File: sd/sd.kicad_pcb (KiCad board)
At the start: 2 copper layers, 76.2 x 50.8 mm, 13 parts, among them J1 Micro_SD_Card_Det2, J2 Conn_01x09, J3 STM32WORLD_BOARD, J4 STM32WORLD_CONNECTOR_1, J5 STM32WORLD_CONNECTOR_2

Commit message: Working on sd
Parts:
- removed J2: Conn_01x09, Connector_PinHeader_2.54mm:PinHeader_1x09_P2.54mm_Vertical
- added JP1: SolderJumper_3_Open, Jumper:SolderJumper-3_P2.0mm_Open_TrianglePad1.0x1.5mm, F.Cu at (171.5, 87.6)
- added JP10: SolderJumper_2_Open, Jumper:SolderJumper-2_P1.3mm_Open_TrianglePad1.0x1.5mm, F.Cu at (151.1, 87.6)
- added JP11: SolderJumper_2_Open, Jumper:SolderJumper-2_P1.3mm_Open_TrianglePad1.0x1.5mm, F.Cu at (139.7, 97.2)
- added JP12: SolderJumper_2_Open, Jumper:SolderJumper-2_P1.3mm_Open_TrianglePad1.0x1.5mm, F.Cu at (143.5, 97.2)
- added JP13: SolderJumper_2_Open, Jumper:SolderJumper-2_P1.3mm_Open_TrianglePad1.0x1.5mm, F.Cu at (147.3, 97.2)
- added JP14: SolderJumper_2_Open, Jumper:SolderJumper-2_P1.3mm_Open_TrianglePad1.0x1.5mm, F.Cu at (151.1, 97.2)
- added JP15: SolderJumper_2_Open, Jumper:SolderJumper-2_P1.3mm_Open_TrianglePad1.0x1.5mm, F.Cu at (139.7, 92.3)
- added JP16: SolderJumper_2_Open, Jumper:SolderJumper-2_P1.3mm_Open_TrianglePad1.0x1.5mm, F.Cu at (143.5, 92.3)
- added JP17: SolderJumper_2_Open, Jumper:SolderJumper-2_P1.3mm_Open_TrianglePad1.0x1.5mm, F.Cu at (147.3, 92.3)
- added JP18: SolderJumper_2_Open, Jumper:SolderJumper-2_P1.3mm_Open_TrianglePad1.0x1.5mm, F.Cu at (151.1, 92.3)
- added JP19: SolderJumper_2_Open, Jumper:SolderJumper-2_P1.3mm_Open_TrianglePad1.0x1.5mm, F.Cu at (139.7, 101.6)
- added JP2: SolderJumper_3_Open, Jumper:SolderJumper-3_P2.0mm_Open_TrianglePad1.0x1.5mm, F.Cu at (171.5, 90.8)
- added JP20: SolderJumper_2_Open, Jumper:SolderJumper-2_P1.3mm_Open_TrianglePad1.0x1.5mm, F.Cu at (143.5, 101.6)
- added JP21: SolderJumper_2_Open, Jumper:SolderJumper-2_P1.3mm_Open_TrianglePad1.0x1.5mm, F.Cu at (147.3, 101.6)
- added JP22: SolderJumper_2_Open, Jumper:SolderJumper-2_P1.3mm_Open_TrianglePad1.0x1.5mm, F.Cu at (151.1, 101.6)
- added JP3: SolderJumper_3_Open, Jumper:SolderJumper-3_P2.0mm_Open_TrianglePad1.0x1.5mm, F.Cu at (171.5, 94.0)
- added JP4: SolderJumper_3_Open, Jumper:SolderJumper-3_P2.0mm_Open_TrianglePad1.0x1.5mm, F.Cu at (171.5, 97.2)
- added JP5: SolderJumper_3_Open, Jumper:SolderJumper-3_P2.0mm_Open_TrianglePad1.0x1.5mm, F.Cu at (171.5, 100.3)
- added JP6: SolderJumper_3_Open, Jumper:SolderJumper-3_P2.0mm_Open_TrianglePad1.0x1.5mm, F.Cu at (171.5, 103.5)
- added JP7: SolderJumper_2_Open, Jumper:SolderJumper-2_P1.3mm_Open_TrianglePad1.0x1.5mm, F.Cu at (139.7, 87.6)
- added JP8: SolderJumper_2_Open, Jumper:SolderJumper-2_P1.3mm_Open_TrianglePad1.0x1.5mm, F.Cu at (143.5, 87.6)
- added JP9: SolderJumper_2_Open, Jumper:SolderJumper-2_P1.3mm_Open_TrianglePad1.0x1.5mm, F.Cu at (147.3, 87.5)
- moved R2 40.8 mm to (176.5, 103.5), turned to 180 degrees
- moved R3 38.8 mm to (176.5, 90.8), turned to 180 degrees
- moved R6 38.5 mm to (176.5, 94.0), turned to 0 degrees
- moved R5 37.5 mm to (176.5, 100.3), turned to 180 degrees
- moved C2 35.5 mm to (188.0, 105.4), turned to 180 degrees
- moved R4 35.0 mm to (176.5, 97.2), turned to 180 degrees
- moved R1 34.7 mm to (176.5, 87.6), turned to 180 degrees
- moved C1 32.8 mm to (188.0, 103.5), turned to 180 degrees
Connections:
- J1 pad 1: /D2 -> /SD_DAT2
- J1 pad 10: /DET -> DET
- J1 pad 2: /D3 -> /SD_DAT3
- J1 pad 3: /CMD -> /SD_CMD
- J1 pad 5: /CLK -> /SD_CLK
- J1 pad 7: /D0 -> /SD_DAT0
- J1 pad 8: /D1 -> /SD_DAT1
- J4 pad 1: unconnected-(J4-GND-Pad1) -> GND
- J4 pad 11: unconnected-(J4-PA3-Pad11) -> SPI2_MOSI
- J4 pad 13: unconnected-(J4-PA5-Pad13) -> SPI1_CLK
- J4 pad 14: unconnected-(J4-PA4-Pad14) -> SPI1_CS
- J4 pad 15: unconnected-(J4-PA7-Pad15) -> SPI1_MOSI
- J4 pad 16: unconnected-(J4-PA6-Pad16) -> SPI1_MISO
- J4 pad 24: unconnected-(J4-PB10-Pad24) -> SPI2_CLK
- J4 pad 26: unconnected-(J4-PB12-Pad26) -> SPI2_CS
- J4 pad 31: unconnected-(J4-PC9-Pad31) -> SDIO_DAT1
- J4 pad 32: unconnected-(J4-PC8-Pad32) -> SDIO_DAT0
- J4 pad 37: unconnected-(J4-GND-Pad37) -> GND
- J4 pad 38: unconnected-(J4-3.3V-Pad38) -> VCC
- J4 pad 39: unconnected-(J4-GND-Pad39) -> GND
- J4 pad 8: unconnected-(J4-PC2-Pad8) -> SPI2_MISO
- J5 pad 1: unconnected-(J5-GND-Pad1) -> GND
- J5 pad 15: unconnected-(J5-PA15-Pad15) -> SPI1A_CS
- J5 pad 19: unconnected-(J5-PC11-Pad19) -> SDIO_DAT3
- J5 pad 20: unconnected-(J5-PC10-Pad20) -> SDIO_DAT2
- J5 pad 22: unconnected-(J5-PC12-Pad22) -> SDIO_CLK
- J5 pad 23: unconnected-(J5-PB3-Pad23) -> SPI1A_CLK
- J5 pad 24: unconnected-(J5-PD2-Pad24) -> SDIO_CMD
- J5 pad 25: unconnected-(J5-PB5-Pad25) -> SPI1A_MOSI
- J5 pad 26: unconnected-(J5-PB4-Pad26) -> SPI1A_MISO
- J5 pad 3: unconnected-(J5-GND-Pad3) -> GND
- J5 pad 35: unconnected-(J5-PC15-Pad35) -> DET
- J5 pad 4: unconnected-(J5-3.3V-Pad4) -> VCC
- R1 pad 2: /D2 -> SDIO_DAT2
- R2 pad 2: /D3 -> SDIO_DAT1
- R3 pad 2: /CMD -> /SD_DAT3
- R4 pad 2: /D0 -> /SD_CMD
- R5 pad 2: /D1 -> /SD_DAT0
- R6 pad 2: /DET -> DET
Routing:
- net DET: track 0.00 -> 66.8 mm
- net SDIO_DAT2: track 0.00 -> 49.5 mm, vias 0 -> 2
- net SPI2_CS: track 0.00 -> 48.0 mm, vias 0 -> 2
- net SPI1_CS: track 0.00 -> 47.0 mm, vias 0 -> 1
- net SDIO_CLK: track 0.00 -> 45.5 mm, vias 0 -> 3
- net SDIO_DAT3: track 0.00 -> 45.2 mm, vias 0 -> 4
- net VCC: track 49.5 -> 93.7 mm
- net SDIO_CMD: track 0.00 -> 42.6 mm, vias 0 -> 2
- net SPI1_MOSI: track 0.00 -> 42.3 mm, vias 0 -> 3
- net /CMD: track 35.2 -> 0.00 mm, vias 1 -> 0
- net /D3: track 34.8 -> 0.00 mm, vias 1 -> 0
- net SPI2_CLK: track 0.00 -> 33.8 mm, vias 0 -> 2
- net /D1: track 33.6 -> 0.00 mm, vias 1 -> 0
- net /D2: track 32.7 -> 0.00 mm, vias 1 -> 0
- net SPI1A_MISO: track 0.00 -> 30.8 mm, vias 0 -> 2
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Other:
- board text removed: "${TITLE}"
- board text removed: "${TITLE} Rev. ${REVISION}"
- board text removed: "(MISO) DO"
- board text removed: "(MOSI) DI"
- board text removed: "CLK"
- board text removed: "CMD"
- board text removed: "CS"
- board text removed: "D0"
- board text removed: "D1"
- board text removed: "D2"
- board text removed: "D3"
- board text removed: "DET"
- board text removed: "GND"
- board text removed: "JLCJLCJLCJLC"
- board text removed: "SCLK"
- board text removed: "SPI"
- board text removed: "VCC"

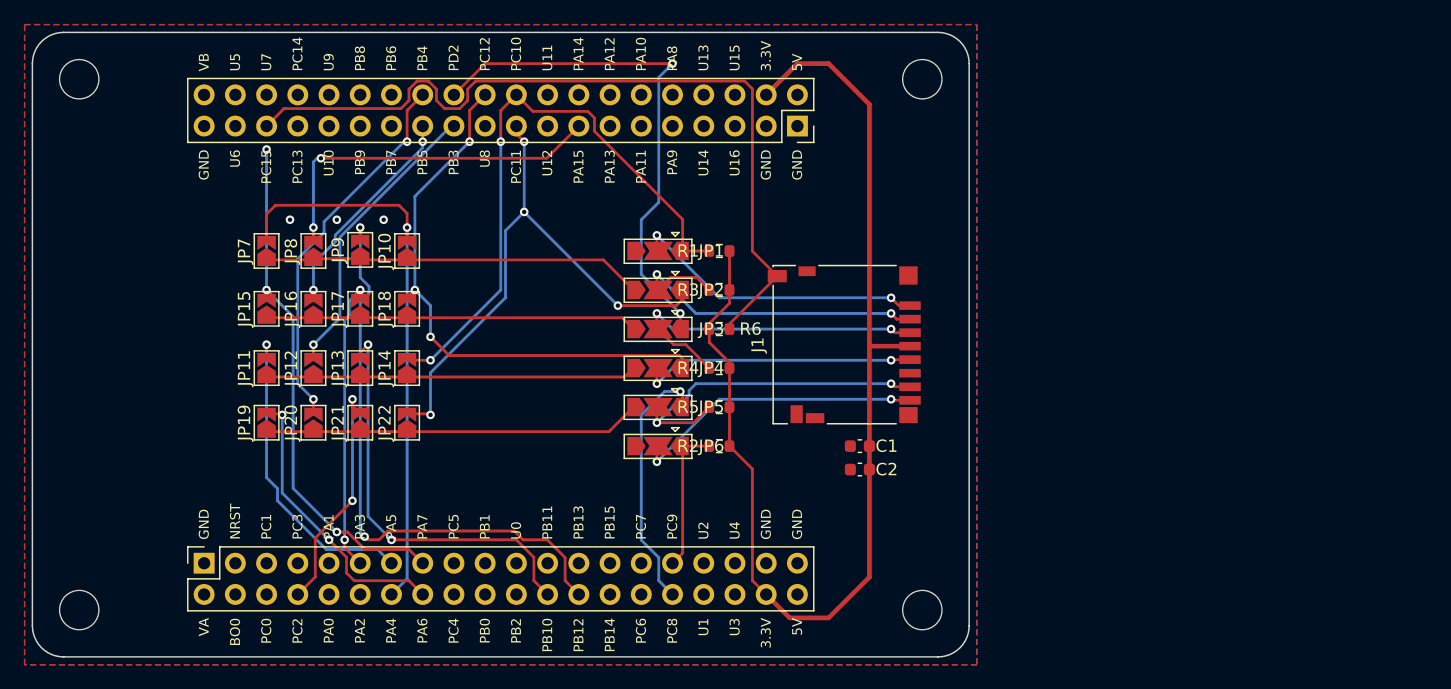
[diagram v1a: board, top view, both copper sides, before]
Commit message: Schematics verified- tweaking pcb
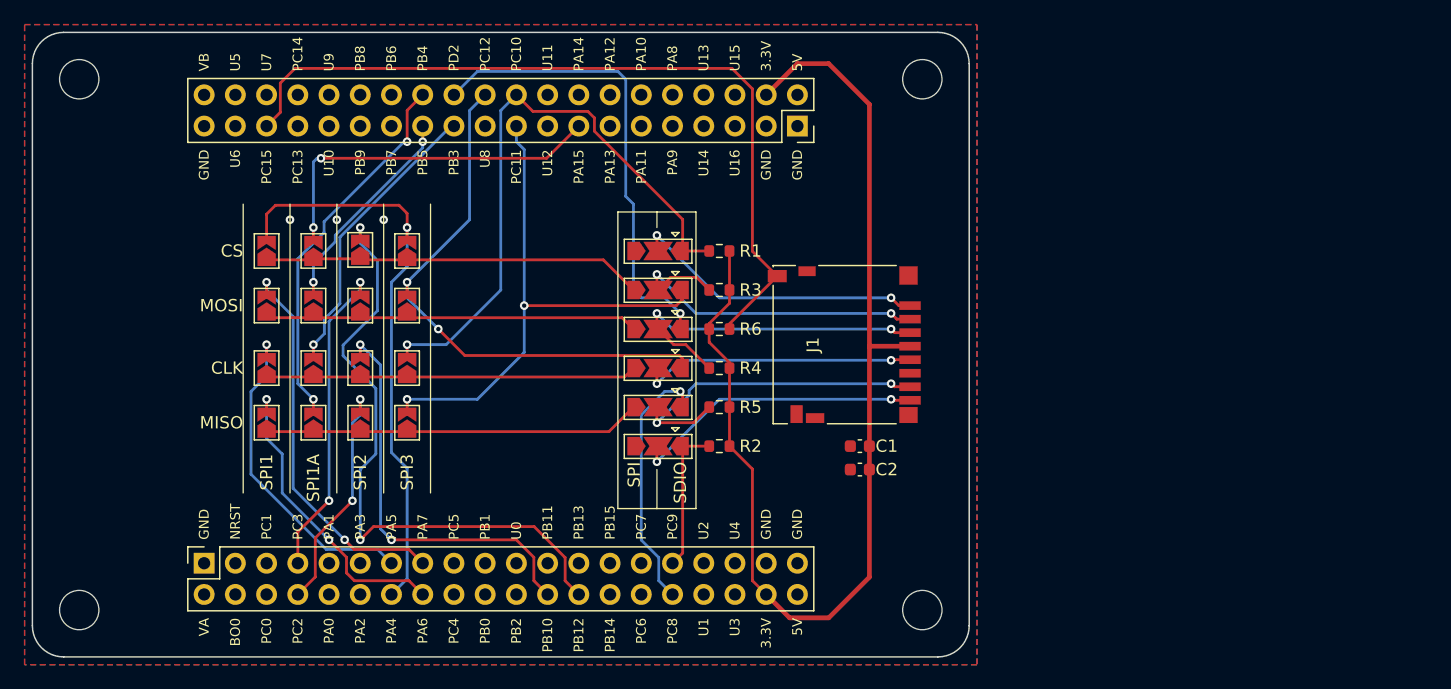
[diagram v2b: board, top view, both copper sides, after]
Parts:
- moved JP15 0.26 mm to (139.7, 92.1)
- moved JP16 0.26 mm to (143.5, 92.1)
- moved JP17 0.26 mm to (147.3, 92.1)
- moved JP18 0.26 mm to (151.1, 92.1)
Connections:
- J4 pad 11: SPI2_MOSI -> unconnected-(J4-PA3-Pad11)
- J4 pad 7: unconnected-(J4-PC3-Pad7) -> SPI2_MOSI
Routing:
- net SPI1_MOSI: track 42.3 -> 31.9 mm, vias 3 -> 2
- net SDIO_CMD: track 42.6 -> 38.1 mm, vias 2 -> 1
- net SPI2_CS: track 48.0 -> 51.5 mm
- net SPI2_MOSI: track 24.1 -> 26.1 mm
- net SPI1_MISO: track 23.3 -> 24.9 mm
- net DET: track 66.8 -> 65.5 mm
- net SPI1_CLK: track 25.6 -> 26.7 mm
- net SPI1_CS: track 47.0 -> 48.0 mm
- net SDIO_DAT2: track 49.5 -> 50.1 mm, vias 2 -> 1
- net SDIO_DAT3: track 45.2 -> 44.8 mm, vias 4 -> 2
- net SDIO_CLK: vias 3 -> 2
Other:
- board text added: "CLK"
- board text added: "CS"
- board text added: "MISO"
- board text added: "MOSI"
- board text added: "SDIO"
- board text added: "SPI"
- board text added: "SPI1"
- board text added: "SPI1A"
- board text added: "SPI2"
- board text added: "SPI3"

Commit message: Ordered sd rev a
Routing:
- net SPI1A_MOSI: track 17.0 -> 17.6 mm, vias 2 -> 1
- net SPI1A_MISO: track 30.8 -> 30.7 mm, vias 2 -> 1
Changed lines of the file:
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@@
 	)
 	(segment
-		(start 144.78 93.345)
-		(end 144.78 107.95)
+		(start 147.32 92.47)
+		(end 147.32 90.17)
 		(width 0.2286)
 		(layer "B.Cu")
@@
 	)
 	(segment
-		(start 147.32 90.805)
-		(end 147.32 90.17)
+		(start 144.78 107.95)
+		(end 144.78 95.01)
 		(width 0.2286)
 		(layer "B.Cu")
@@
 	)
 	(segment
-		(start 147.32 90.805)
-		(end 144.78 93.345)
+		(start 144.78 95.01)
+		(end 147.32 92.47)
 		(width 0.2286)
 		(layer "B.Cu")
@@
 	)
 	(segment
+		(start 143.51 100.875)
+		(end 143.51 99.695)
+		(width 0.2286)
+		(layer "F.Cu")
+		(net 52)
+	)
+	(via
+		(at 143.51 99.695)
+		(size 0.7)
+		(drill 0.35)
+		(layers "F.Cu" "B.Cu")
+		(locked yes)
+		(net 52)
+	)
+	(segment
+		(start 151.13 78.46684)
+		(end 151.13 76.2)
+		(width 0.2286)
+		(layer "B.Cu")
+		(net 52)
+	)
+	(segment
+		(start 142.24 98.425)
+		(end 142.24 88.265)
+		(width 0.2286)
+		(layer "B.Cu")
+		(net 52)
+	)
+	(segment
+		(start 142.24 88.265)
+		(end 144.1277 86.3773)
+		(width 0.2286)
+		(layer "B.Cu")
+		(net 52)
+	)
+	(segment
 		(start 151.13 76.2)
 		(end 152.4 74.93)
 		(width 0.2286)
-		(layer "F.Cu")
+		(layer "B.Cu")
 		(net 52)
 	)
 	(segment
-		(start 151.13 78.74)
-		(end 151.13 76.2)
-		(width 0.2286)
-		(layer "F.Cu")
-		(net 52)
-	)
-	(segment
-		(start 143.51 100.875)
-		(end 143.51 99.695)
-		(width 0.2286)
-		(layer "F.Cu")
-		(net 52)
-	)
-	(via
-		(at 143.51 99.695)
-		(size 0.7)
-		(drill 0.35)
-		(layers "F.Cu" "B.Cu")
-		(locked yes)
-		(net 52)
-	)
-	(via
-		(at 151.13 78.74)
-		(size 0.7)
-		(drill 0.35)
-		(layers "F.Cu" "B.Cu")
-		(net 52)
-	)
-	(segment
-		(start 142.24 98.425)
-		(end 142.24 88.265)
+		(start 144.1277 86.3773)
+		(end 144.1277 85.46914)
 		(width 0.2286)
 		(layer "B.Cu")
@@
 	)
 	(segment
-		(start 144.375398 85.256042)
-		(end 150.89144 78.74)
-		(width 0.2286)
-		(layer "B.Cu")
-		(net 52)
-	)
-	(segment
-		(start 142.24 88.265)
-		(end 144.375398 86.129602)
-		(width 0.2286)
-		(layer "B.Cu")
-		(net 52)
-	)
-	(segment
-		(start 144.375398 86.129602)
-		(end 144.375398 85.256042)
-		(width 0.2286)
-		(layer "B.Cu")
-		(net 52)
-	)
-	(segment
-		(start 150.89144 78.74)
-		(end 151.13 78.74)
+		(start 144.1277 85.46914)
+		(end 151.13 78.46684)
 		(width 0.2286)
 		(layer "B.Cu")
@@
 		(net 87)
 	)
-	(segment
-		(start 152.4 78.74)
-		(end 152.4 78.01023)
-		(width 0.2286)
-		(layer "F.Cu")
+	(via
+		(at 143.51 90.17)
+		(size 0.7)
+		(drill 0.35)
+		(layers "F.Cu" "B.Cu")
+		(locked yes)
 		(net 87)
 	)
-	(via
-		(at 143.51 90.17)
-		(size 0.7)
-		(drill 0.35)
-		(layers "F.Cu" "B.Cu")
-		(locked yes)
+	(segment
+		(start 143.51 90.17)
+		(end 145.287 88.393)
+		(width 0.2286)
+		(layer "B.Cu")
 		(net 87)
 	)
-	(via
-		(at 152.4 78.74)
-		(size 0.7)
-		(drill 0.35)
-		(layers "F.Cu" "B.Cu")
+	(segment
+		(start 145.287 86.345624)
+		(end 152.4 79.232624)
+		(width 0.2286)
+		(layer "B.Cu")
 		(net 87)
 	)
 	(segment
-		(start 145.287 86.88444)
-		(end 143.51 88.66144)
+		(start 152.4 79.232624)
+		(end 152.4 77.47)
 		(width 0.2286)
 		(layer "B.Cu")
@@
 	)
 	(segment
-		(start 152.4 79.232624)
+		(start 145.287 88.393)
 		(end 145.287 86.345624)
 		(width 0.2286)
 		(layer "B.Cu")
-		(net 87)
-	)
-	(segment
-		(start 145.287 86.345624)
-		(end 145.287 86.88444)
-		(width 0.2286)
-		(layer "B.Cu")
-		(net 87)
-	)
-	(segment
-		(start 143.51 88.66144)
-		(end 143.51 90.17)
-		(width 0.2286)
-		(layer "B.Cu")
-		(net 87)
-	)
-	(segment
-		(start 152.4 78.74)
-		(end 152.4 79.232624)
-		(width 0.2286)
-		(layer "B.Cu")
